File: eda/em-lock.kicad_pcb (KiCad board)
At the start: 2 copper layers, 75 x 75 mm, 62 parts, among them CON1 BARREL_JACK, P1 BTN_CALL, P10 EXT_LED_CONN, P2 BTN_OPEN, P3 BOOT_SEL_CONN, P4 LOCK_CONN, P5 PWR_SELECT, P6 PWR_SW_CONN, P7 SWD_CONN, P8 ESP8266_CONN, P9 USB_B, Q1 Q_NMOS_DGS, Q2 MMBT3906, Q3 MMBT3906, Q4 MMBT3906, SW1 RST_BTN, U1 74LVC2G14, U2 STM32F103C8Tx, U3 LD1117S33CTR, Y1 8MHz

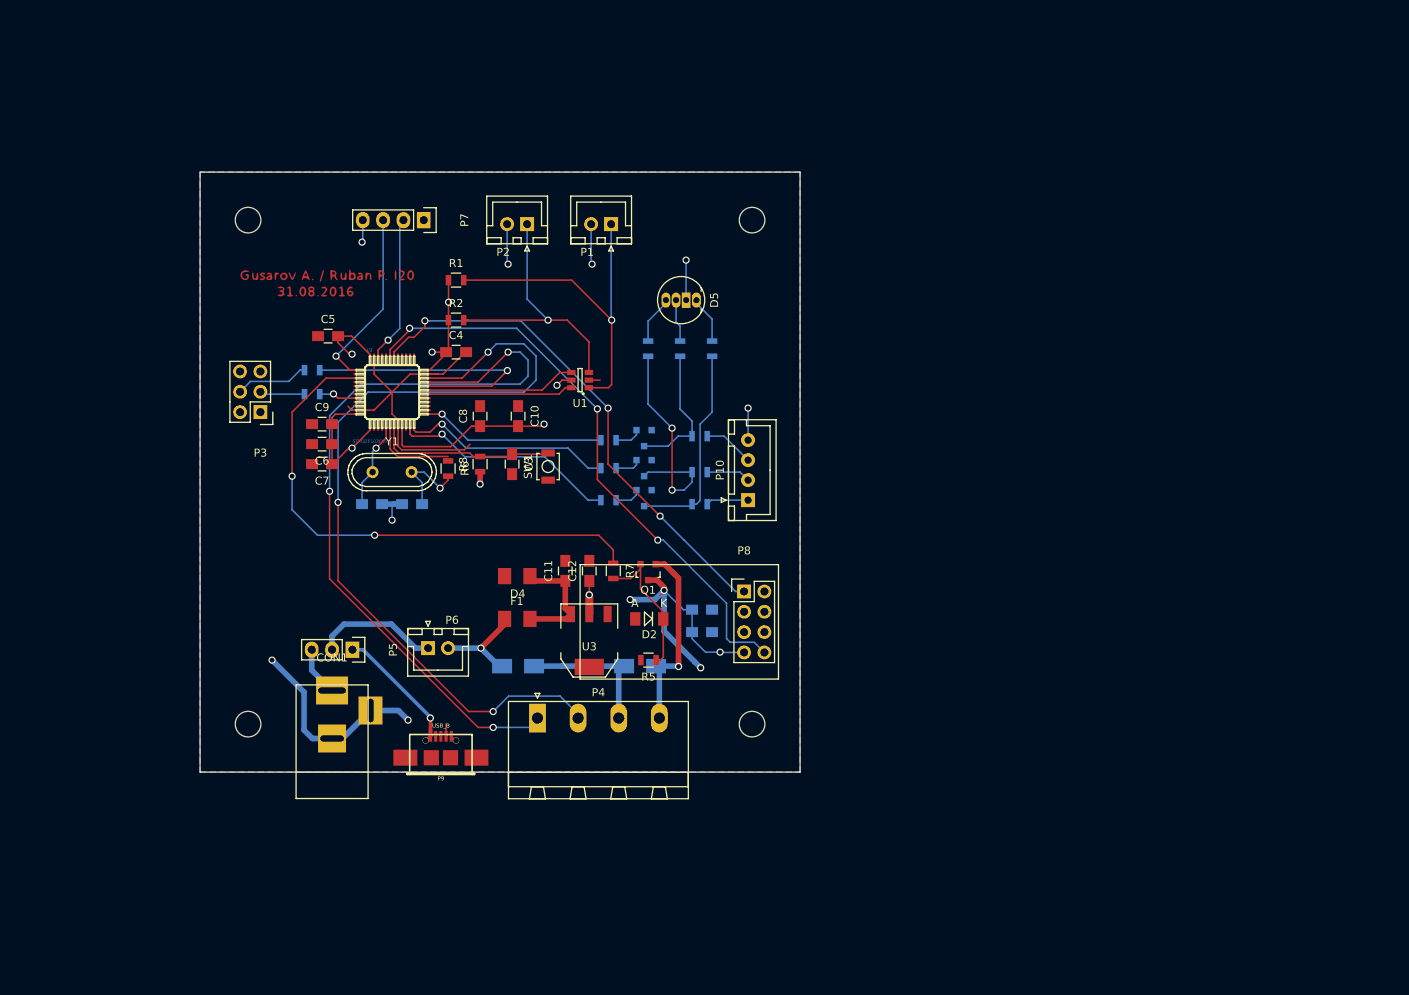
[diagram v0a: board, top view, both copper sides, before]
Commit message: refs #41563 fix stable schematics version
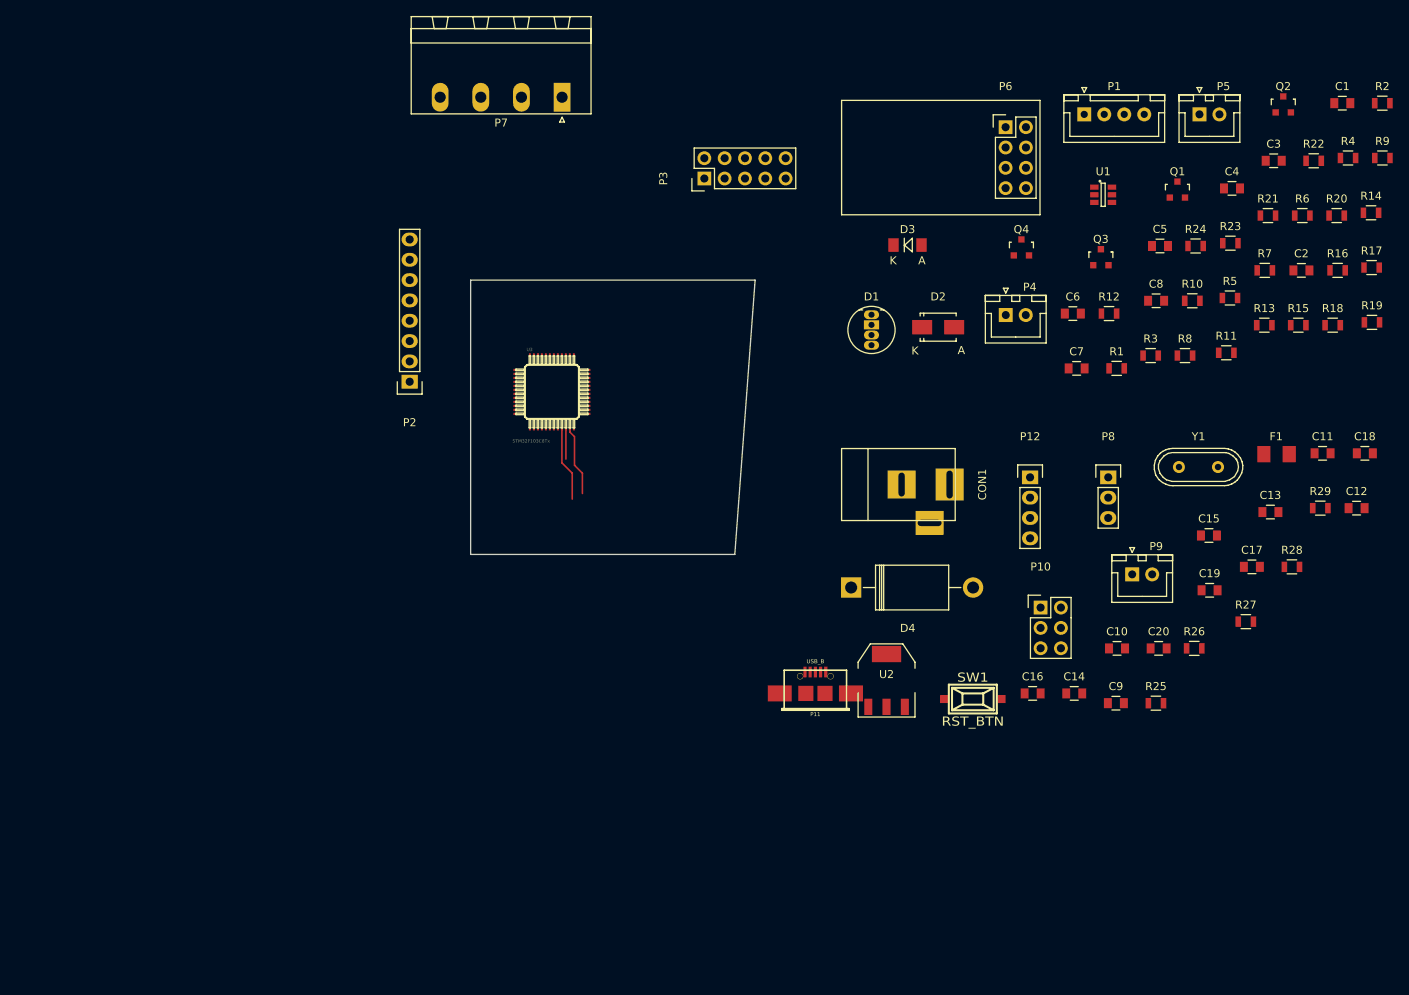
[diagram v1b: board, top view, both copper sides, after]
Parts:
- removed D5: LED_RCBG, I20:LED-RGB-5MM_Common_Cathode
- removed G1: LOGO, common_parts:logo_2016
- removed HOLE1, HOLE2, HOLE3, HOLE4: MountingHole_3.2mm_M3, Mounting_Holes:MountingHole_3.2mm_M3
- added C15: 2pF, I20:C_0805, F.Cu at (176.1, 95.4)
- added C16: 100nF, I20:C_0805, F.Cu at (154.1, 115.2)
- added C17: 100nF, I20:C_0805, F.Cu at (181.5, 99.3)
- added C18: 100nF, I20:C_0805, F.Cu at (195.6, 85.2)
- added C19: 10uF, I20:C_0805, F.Cu at (176.2, 102.3)
- added C20: 1uF, I20:C_0805, F.Cu at (169.8, 109.5)
- added P11: USB_B, I20:conn_usb_B_micro_smd-2, F.Cu at (126.9, 115.2)
- added P12: SWD_CONN, I20:Pin_Header_Straight_1x04, F.Cu at (153.8, 88.2)
- added R18: 4.7k, I20:R_0805, F.Cu at (191.6, 69.1)
- added R19: 4.7k, I20:R_0805, F.Cu at (196.5, 68.8)
- added R20: 4.7k, I20:R_0805, F.Cu at (192.1, 55.4)
- added R21: 4.7k, I20:R_0805, F.Cu at (183.5, 55.4)
- added R22: 0, I20:R_0805, F.Cu at (189.2, 48.6)
- added R23: 10k, I20:R_0805, F.Cu at (178.8, 58.9)
- added R24: 240, I20:R_0805, F.Cu at (174.4, 59.2)
- added R25: 10k, I20:R_0805, F.Cu at (169.5, 116.4)
- added R26: 10k, I20:R_0805, F.Cu at (174.3, 109.5)
- added R27: 10k, I20:R_0805, F.Cu at (180.7, 106.2)
- added R28: 0R, I20:R_0805, F.Cu at (186.5, 99.3)
- added R29: 0, I20:R_0805, F.Cu at (190.0, 92.0)
- C1: value 2pF -> 100nF; footprint I20:C_0805_HandSoldering -> I20:C_0805; moved to F.Cu
- C10: value 1uF -> 100nF; footprint I20:C_0805_HandSoldering -> I20:C_0805
- C11, C12, C3, C7: footprint I20:C_0805_HandSoldering -> I20:C_0805
- C13: value 10uF -> 100nF; footprint I20:C_0805_HandSoldering -> I20:C_0805; moved to F.Cu
- C14: value 100nF -> 2pF; footprint I20:C_0805_HandSoldering -> I20:C_0805; moved to F.Cu
- C2: value 2pF -> 10uF; footprint I20:C_0805_HandSoldering -> I20:C_0805; moved to F.Cu
- C4, C5: value 100nF -> 0; footprint I20:C_0805_HandSoldering -> I20:C_0805
- C6, C8: value 100nF -> 10uF; footprint I20:C_0805_HandSoldering -> I20:C_0805
- C9: value 10uF -> 100nF; footprint I20:C_0805_HandSoldering -> I20:C_0805
- D1: value M7 -> LED_RCBG; footprint I20:SMA_Standard -> I20:LED-RGB-5MM_Common_Cathode; moved to F.Cu
- D2: value ZENER-MOSFET-GATE -> M7; footprint I20:MiniMELF_Standard -> I20:SMA_Standard
- D3: value D_Schottky -> ZENER-MOSFET-GATE; footprint I20:SMA_Standard -> I20:MiniMELF_Standard; moved to F.Cu
- D4: footprint I20:Fuse_SMD1206_Wave -> Diodes_ThroughHole:Diode_DO-201AD_Horizontal_RM15
- P1: value BTN_CALL -> EXT_LED_CONN; footprint I20:JST_XH_B02B-XH-A_02x2.50mm_Straight -> I20:JST_XH_B04B-XH-A_04x2.50mm_Straight
- P10: value EXT_LED_CONN -> BOOT_SEL_CONN; footprint I20:JST_XH_B04B-XH-A_04x2.50mm_Straight -> I20:Pin_Header_Straight_2x03
- P2: value BTN_OPEN -> RC522A; footprint I20:JST_XH_B02B-XH-A_02x2.50mm_Straight -> Pin_Headers:Pin_Header_Straight_1x08
- P3: value BOOT_SEL_CONN -> RC522B; footprint I20:Pin_Header_Straight_2x03 -> Pin_Headers:Pin_Header_Straight_2x05
- P4: value LOCK_CONN -> BTN_OPEN; footprint I20:PhoenixContact_MSTBA-G_04x5.08mm_Angled -> I20:JST_XH_B02B-XH-A_02x2.50mm_Straight
- P5: value PWR_SELECT -> BTN_CALL; footprint I20:Pin_Header_Straight_1x03 -> I20:JST_XH_B02B-XH-A_02x2.50mm_Straight
- P6: value PWR_SW_CONN -> ESP8266_CONN; footprint I20:JST_XH_B02B-XH-A_02x2.50mm_Straight -> I20:ESP8266_CONN
- P7: value SWD_CONN -> LOCK_CONN; footprint I20:Pin_Header_Straight_1x04 -> I20:PhoenixContact_MSTBA-G_04x5.08mm_Angled
- P8: value ESP8266_CONN -> PWR_SELECT; footprint I20:ESP8266_CONN -> I20:Pin_Header_Straight_1x03
- P9: value USB_B -> PWR_SW_CONN; footprint I20:conn_usb_B_micro_smd-2 -> I20:JST_XH_B02B-XH-A_02x2.50mm_Straight
- Q1: value Q_NMOS_DGS -> MMBT3906
- Q2, Q3, R11: moved to F.Cu
- Q4: value MMBT3906 -> Q_NMOS_DGS; moved to F.Cu
- R1: value 10k -> 10R
- R10: value 2k -> 82R; moved to F.Cu
- R12: value 82R -> 2k; moved to F.Cu
- R13: value 15R -> 2k; moved to F.Cu
- R14: value 10R -> 10k; moved to F.Cu
- R15: value 82R -> 10k; moved to F.Cu
- R16: value 15R -> 0; moved to F.Cu
- R17: value 10R -> 0; moved to F.Cu
- R2: value 10k -> 15R
- R3: value 10k -> 82R; moved to F.Cu
- R4: value 10k -> 4.7k; moved to F.Cu
- R5, R8: value 10k -> 4.7k
- R6: value 0R -> 10R
- R7: value 240 -> 4.7k
- R9: value 2k -> 15R; moved to F.Cu
- SW1: footprint Buttons_Switches_SMD:SW_SPST_B3U-1000P -> I20:smd_push
- U2: value STM32F103C8Tx -> LD1117S33CTR; footprint I20:SparkFun-LQFP-48 -> I20:SOT-223
- U3: value LD1117S33CTR -> STM32F103C8Tx; footprint I20:SOT-223 -> I20:SparkFun-LQFP-48
- moved R4 132.2 mm to (193.5, 48.2)
- moved C1 131.2 mm to (192.8, 41.4)
- moved P5 125.3 mm to (174.9, 42.8), turned to 0 degrees
- moved R2 118.9 mm to (197.8, 41.4)
- moved C2 114.9 mm to (187.7, 62.3), turned to 0 degrees
- moved R6 111.4 mm to (187.8, 55.4), turned to 0 degrees
- moved R9 105.8 mm to (197.8, 48.2), turned to 0 degrees
- moved C9 105.2 mm to (164.5, 116.4)
- moved R3 104.9 mm to (168.8, 72.9)
- moved C5 104.6 mm to (170.0, 59.2)
- moved C3 102.5 mm to (184.2, 48.6), turned to 0 degrees
- moved Y1 100.8 mm to (174.8, 86.9)
- moved C4 99.1 mm to (179.0, 52.0)
- moved P6 98.0 mm to (155.0, 48.2)
- moved F1 97.1 mm to (184.6, 85.3)
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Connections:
- C1 pad 1: /OSC_IN -> VCC
- C1 pad 2: GND -> GNDD
- C10 pad 1: GND -> VCC
- C10 pad 2: VCC -> GND
- C11 pad 1: /LDO_IN -> /stm32f103c8/LDO_IN
- C14 pad 1: GND -> /stm32f103c8/PD0/RCC_OSC_IN
- C14 pad 2: VCC -> Net-(C14-Pad2)
- C2 pad 1: /OSC_OUT -> VCC
- C2 pad 2: GND -> GNDD
- C3 pad 1: /NRST -> VCC
- C3 pad 2: GND -> GNDD
- C4 pad 1: VCC -> GNDD
- C4 pad 2: GND -> Net-(C4-Pad2)
- C5 pad 1: GND -> GNDD
- C5 pad 2: VCC -> Net-(C5-Pad2)
- C6 pad 2: GND -> GNDD
- C7 pad 1: VCC -> GNDD
- C7 pad 2: GND -> VCC
- C8 pad 1: VCC -> GNDD
- C8 pad 2: GND -> VCC
- C9 pad 1: GND -> /stm32f103c8/NRST
- C9 pad 2: VCC -> GND
- CON1 pad 1: /12V_EXT -> /stm32f103c8/12V_EXT
- D1 pad 1: EM_LOCK -> Net-(D1-Pad1)
- D1 pad 2: /LOCK_GND -> GND
- D2 pad 1: Net-(D2-Pad1) -> EM_LOCK
- D2 pad 2: GND -> LOCK_GND
- D3 pad 1: EM_LOCK -> Net-(D3-Pad1)
- D3 pad 2: /PWR_UNFUSED -> GND
- D4 pad 1: /LDO_IN -> /stm32f103c8/LDO_IN
- F1 pad 1: /PWR_UNFUSED -> Net-(F1-Pad1)
- F1 pad 2: /LDO_IN -> Net-(F1-Pad2)
- P1 pad 2: GND -> Net-(P1-Pad2)
- P10 pad 2: Net-(P10-Pad2) -> Net-(P10-Pad1)
- P10 pad 4: GND -> Net-(P10-Pad4)
- P2 pad 1: Net-(P2-Pad1) -> /PB5_RC522A_CS
- P2 pad 2: GND -> /PB13_SPI2_SCK
- P3 pad 1: VCC -> /PB6_RC522B_CS
- P3 pad 2: VCC -> /PB13_SPI2_SCK
- P3 pad 3: Net-(P3-Pad3) -> /PB15_SPI2_MOSI
- P3 pad 4: Net-(P3-Pad4) -> /PB14_SPI2_MISO
- P3 pad 5: GND -> /PB9_RC522B_IRQ
- P3 pad 6: GND -> GNDD
- P4 pad 1: /UART_EXT_TX -> Net-(P4-Pad1)
- P4 pad 2: /UART_EXT_RX -> GNDD
- P5 pad 1: +5V -> Net-(P5-Pad1)
- P5 pad 2: Net-(P5-Pad2) -> GNDD
- P6 pad 1: Net-(P5-Pad2) -> (no net)
- P6 pad 2: /PWR_UNFUSED -> VCC
- P7 pad 1: VCC -> (no net)
- P7 pad 2: Net-(P7-Pad2) -> (no net)
- P7 pad 3: Net-(P7-Pad3) -> EM_LOCK
- P7 pad 4: GND -> LOCK_GND
- P8 pad 1: /UART_INT_TX -> /stm32f103c8/12V_EXT
- P8 pad 2: VCC -> Net-(F1-Pad2)
- P8 pad 3: Net-(P8-Pad3) -> +5V
- P9 pad 1: +5V -> /stm32f103c8/LDO_IN
- Q1 pad 1: /LOCK_GND -> Net-(Q1-Pad1)
- Q1 pad 2: Net-(D2-Pad1) -> VCC
- Q1 pad 3: GND -> Net-(Q1-Pad3)
- Q4 pad 1: Net-(Q4-Pad1) -> LOCK_GND
- Q4 pad 2: VCC -> Net-(D3-Pad1)
- Q4 pad 3: Net-(Q4-Pad3) -> GND
- R1 pad 1: VCC -> Net-(Q1-Pad3)
- R1 pad 2: Net-(P1-Pad1) -> Net-(P1-Pad3)
- R10 pad 1: Net-(Q3-Pad1) -> Net-(Q3-Pad3)
- R10 pad 2: /PIN_GREEN -> Net-(D1-Pad1)
- R11 pad 1: Net-(Q4-Pad1) -> Net-(Q1-Pad1)
- R11 pad 2: /PIN_BLUE -> (no net)
- R12 pad 1: Net-(Q2-Pad3) -> Net-(Q2-Pad1)
- R12 pad 2: Net-(D5-Pad1) -> (no net)
- R13 pad 1: Net-(Q3-Pad3) -> Net-(Q3-Pad1)
- R13 pad 2: Net-(D5-Pad4) -> (no net)
- R14 pad 1: Net-(Q4-Pad3) -> VCC
- R14 pad 2: Net-(D5-Pad3) -> Net-(P4-Pad1)
- R15 pad 1: Net-(Q2-Pad3) -> VCC
- R15 pad 2: Net-(P10-Pad1) -> Net-(P5-Pad1)
- R16 pad 1: Net-(Q3-Pad3) -> Net-(C4-Pad2)
- R16 pad 2: Net-(P10-Pad2) -> Net-(P4-Pad1)
- R17 pad 1: Net-(Q4-Pad3) -> Net-(C5-Pad2)
- R17 pad 2: Net-(P10-Pad3) -> Net-(P5-Pad1)
- R2 pad 1: VCC -> Net-(Q2-Pad3)
- R2 pad 2: Net-(P2-Pad1) -> Net-(P1-Pad2)
- R3 pad 1: Net-(P3-Pad3) -> Net-(Q3-Pad3)
- R3 pad 2: /BOOT0 -> Net-(P1-Pad1)
- R4 pad 1: Net-(P3-Pad4) -> VCC
- R4 pad 2: /BOOT1 -> /PB5_RC522A_CS
- R5 pad 1: Net-(D2-Pad1) -> VCC
- R5 pad 2: GND -> /PB14_SPI2_MISO
- R6 pad 1: Net-(R6-Pad1) -> Net-(Q1-Pad3)
- R6 pad 2: /OSC_OUT -> Net-(D1-Pad3)
- R7 pad 1: /LOCK_OPEN -> GNDD
- R7 pad 2: Net-(D2-Pad1) -> /PB8_RC522A_IRQ
- R8 pad 2: /NRST -> /PB7_RC522_RST
- R9 pad 1: Net-(Q2-Pad1) -> Net-(Q2-Pad3)
- R9 pad 2: /PIN_RED -> Net-(D1-Pad4)
- SW1 pad 2: /NRST -> /stm32f103c8/NRST
- U1 pad 1: Net-(P1-Pad1) -> Net-(C4-Pad2)
- U1 pad 3: Net-(P2-Pad1) -> Net-(C5-Pad2)
- U1 pad 4: /BTN_CALL -> (no net)
- U1 pad 6: /BTN_OPEN -> (no net)
- U2 pad 1: VCC -> GND
- U2 pad 2: Net-(U2-Pad2) -> VCC
- U2 pad 3: Net-(U2-Pad3) -> /stm32f103c8/LDO_IN
- U2 pad 4: Net-(U2-Pad4) -> (no net)
- U3 pad 1: GND -> VCC
- U3 pad 2: VCC -> (no net)
- U3 pad 3: /LDO_IN -> (no net)
- Y1 pad 1: /OSC_IN -> /stm32f103c8/PD0/RCC_OSC_IN
- Y1 pad 2: /OSC_OUT -> Net-(C15-Pad1)
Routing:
- net GND: track 131.9 -> 0.00 mm, vias 12 -> 0
- net /UART_EXT_RX: track 105.2 -> 0.00 mm, vias 3 -> 0
- net /UART_EXT_TX: track 98.5 -> 0.00 mm, vias 3 -> 0
- net /UART_INT_RX: track 73.6 -> 0.00 mm, vias 3 -> 0
- net /LOCK_OPEN: track 66.1 -> 0.00 mm, vias 2 -> 0
- net /UART_INT_TX: track 64.7 -> 0.00 mm, vias 3 -> 0
- net (no net): track 0.00 -> 59.6 mm
- net VCC: track 68.4 -> 9.69 mm, vias 8 -> 0
- net Net-(P1-Pad1): track 43.8 -> 0.00 mm, vias 1 -> 0
- net /BOOT1: track 34.5 -> 0.00 mm, vias 1 -> 0
- net Net-(P2-Pad1): track 34.3 -> 0.00 mm, vias 1 -> 0
- net /PIN_RED: track 28.5 -> 0.00 mm, vias 1 -> 0
- net Net-(Q3-Pad3): track 28.3 -> 0.00 mm, vias 2 -> 0
- net /PIN_GREEN: track 26.6 -> 0.00 mm, vias 1 -> 0
- net Net-(Q2-Pad3): track 25.9 -> 0.00 mm
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- removed copper zone on F.Cu, net GND
- removed copper zone on B.Cu, net VCC
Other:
- board size 75 x 75 mm -> 35.6 x 34.3 mm

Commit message: refs #41563 pcb projecting half-done
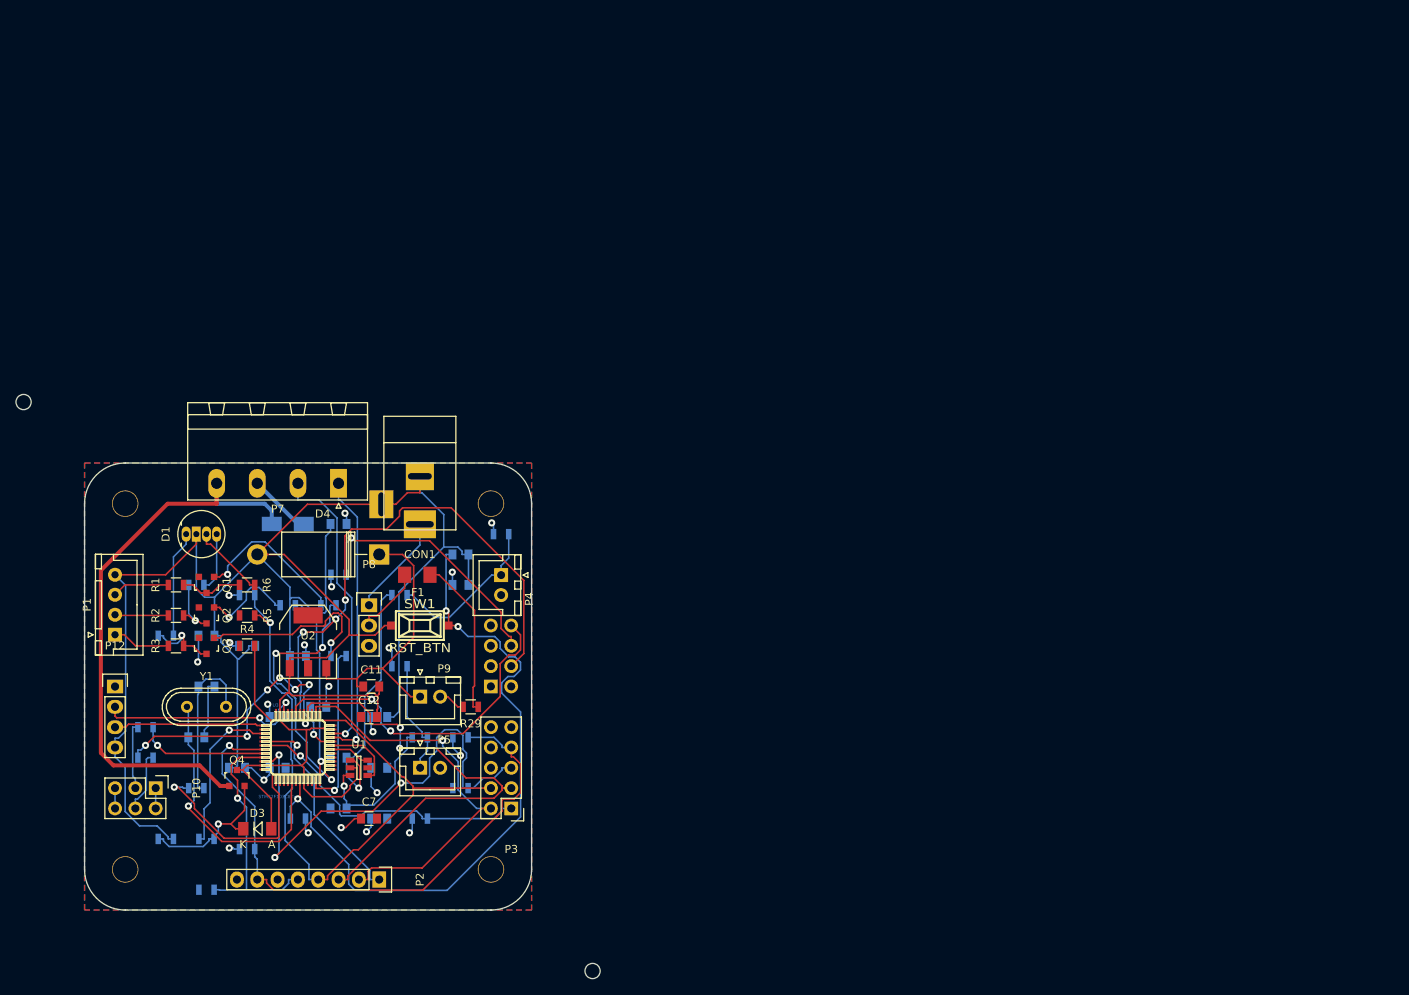
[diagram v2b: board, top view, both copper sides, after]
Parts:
- removed P11: USB_B, I20:conn_usb_B_micro_smd-2
- added H1: MountingHole_3.1mm, I20:MountingHole_3.1mm, F.Cu at (40.6, 91.4)
- added H2: MountingHole_3.1mm, I20:MountingHole_3.1mm, F.Cu at (86.4, 91.4)
- added H3: MountingHole_3.1mm, I20:MountingHole_3.1mm, F.Cu at (86.4, 137.2)
- added H4: MountingHole_3.1mm, I20:MountingHole_3.1mm, F.Cu at (40.6, 137.2)
- added H5: MountingHole_1.9mm, I20:MountingHole_1.9mm, F.Cu at (99.1, 149.9)
- added H6: MountingHole_1.9mm, I20:MountingHole_1.9mm, F.Cu at (27.9, 78.7)
- C1, C10, C13, C14, C15, C16, C17, C18, C19, C2, C20, C3, C4, C5, C6, C8, C9, D2, R10, R11, R12, R13, R14, R15, R16, R17, R18, R19, R20, R21, R22, R23, R24, R25, R26, R27, R28, R7, R8, R9: moved to B.Cu
- F1: value F_Small -> 3A
- P6: footprint I20:ESP8266_CONN -> ESP8266_CONN; moved to B.Cu
- moved R2 163.8 mm to (47.0, 105.4), turned to 180 degrees
- moved R9 157.6 mm to (49.5, 101.6)
- moved C1 153.6 mm to (59.7, 118.1)
- moved R7 153.3 mm to (50.8, 139.7)
- moved R23 152.5 mm to (45.7, 133.3)
- moved R4 150.5 mm to (55.9, 109.2)
- moved Q2 149.0 mm to (50.8, 105.4), turned to 180 degrees
- moved R19 144.7 mm to (55.9, 102.9)
- moved R24 144.2 mm to (50.8, 133.3)
- moved C2 142.3 mm to (59.7, 124.5)
- moved R6 139.7 mm to (55.9, 101.6)
- moved R28 139.7 mm to (49.5, 127.0)
- moved R27 138.6 mm to (43.2, 123.2)
- moved P1 137.5 mm to (39.4, 107.8), turned to 90 degrees
- moved C3 135.1 mm to (72.4, 124.5)
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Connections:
- P2 pad 1: /PB5_RC522A_CS -> PB5_RC522A_CS
- P2 pad 2: /PB13_SPI2_SCK -> PB13_SPI2_SCK
- P2 pad 3: /PB15_SPI2_MOSI -> PB15_SPI2_MOSI
- P2 pad 4: /PB14_SPI2_MISO -> PB14_SPI2_MISO
- P2 pad 5: /PB8_RC522A_IRQ -> PB8_RC522A_IRQ
- P2 pad 7: /PB7_RC522_RST -> PB7_RC522_RST
- P3 pad 1: /PB6_RC522B_CS -> PB6_RC522B_CS
- P3 pad 10: (no net) -> Net-(P3-Pad10)
- P3 pad 2: /PB13_SPI2_SCK -> PB13_SPI2_SCK
- P3 pad 3: /PB15_SPI2_MOSI -> PB15_SPI2_MOSI
- P3 pad 4: /PB14_SPI2_MISO -> PB14_SPI2_MISO
- P3 pad 5: /PB9_RC522B_IRQ -> PB9_RC522B_IRQ
- P3 pad 7: /PB7_RC522_RST -> PB7_RC522_RST
- P3 pad 9: (no net) -> Net-(P3-Pad9)
- P6 pad 1: (no net) -> UART_INT_TX
- P6 pad 3: (no net) -> Net-(P6-Pad3)
- P6 pad 4: (no net) -> ESP_RESET
- P6 pad 5: (no net) -> Net-(P6-Pad5)
- P6 pad 8: (no net) -> UART_INT_RX
- P7 pad 1: (no net) -> UART_EXT_TX
- P7 pad 2: (no net) -> UART_EXT_RX
- P8 pad 3: +5V -> Net-(P8-Pad3)
- R11 pad 2: (no net) -> PIN_BLUE
- R12 pad 2: (no net) -> PIN_GREEN
- R13 pad 2: (no net) -> PIN_RED
- R18 pad 2: /PB6_RC522B_CS -> PB6_RC522B_CS
- R19 pad 2: /PB14_SPI2_MISO -> PB14_SPI2_MISO
- R20 pad 2: /PB9_RC522B_IRQ -> PB9_RC522B_IRQ
- R21 pad 2: /PB7_RC522_RST -> PB7_RC522_RST
- R24 pad 1: (no net) -> LOCK_OPEN
- R4 pad 2: /PB5_RC522A_CS -> PB5_RC522A_CS
- R5 pad 2: /PB14_SPI2_MISO -> PB14_SPI2_MISO
- R7 pad 2: /PB8_RC522A_IRQ -> PB8_RC522A_IRQ
- R8 pad 2: /PB7_RC522_RST -> PB7_RC522_RST
- U1 pad 4: (no net) -> BTN_CALL
- U1 pad 6: (no net) -> BTN_OPEN
- U3 pad 10: (no net) -> Net-(U3-Pad10)
- U3 pad 11: (no net) -> PIN_RED
- U3 pad 12: (no net) -> PIN_GREEN
- U3 pad 13: (no net) -> PIN_BLUE
- U3 pad 14: (no net) -> Net-(U3-Pad14)
- U3 pad 15: (no net) -> Net-(U3-Pad15)
- U3 pad 16: (no net) -> Net-(U3-Pad16)
- U3 pad 17: (no net) -> Net-(U3-Pad17)
- U3 pad 18: (no net) -> BTN_OPEN
- U3 pad 19: (no net) -> BTN_CALL
- U3 pad 2: (no net) -> Net-(U3-Pad2)
- U3 pad 21: (no net) -> UART_EXT_TX
- U3 pad 22: (no net) -> UART_EXT_RX
- U3 pad 25: (no net) -> Net-(U3-Pad25)
- U3 pad 26: (no net) -> PB13_SPI2_SCK
- U3 pad 27: (no net) -> PB14_SPI2_MISO
- U3 pad 28: (no net) -> PB15_SPI2_MOSI
- U3 pad 29: (no net) -> ESP_RESET
- U3 pad 3: (no net) -> Net-(U3-Pad3)
- U3 pad 30: (no net) -> UART_INT_TX
- U3 pad 31: (no net) -> UART_INT_RX
- U3 pad 32: (no net) -> Net-(U3-Pad32)
- U3 pad 33: (no net) -> Net-(U3-Pad33)
- U3 pad 38: (no net) -> Net-(U3-Pad38)
- U3 pad 39: (no net) -> LOCK_OPEN
- U3 pad 4: (no net) -> Net-(U3-Pad4)
- U3 pad 40: (no net) -> Net-(U3-Pad40)
- U3 pad 41: (no net) -> PB5_RC522A_CS
- U3 pad 42: (no net) -> PB6_RC522B_CS
- U3 pad 43: (no net) -> PB7_RC522_RST
- U3 pad 45: (no net) -> PB8_RC522A_IRQ
- U3 pad 46: (no net) -> PB9_RC522B_IRQ
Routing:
- net GND: track 0.00 -> 292.6 mm
- net PB14_SPI2_MISO: track 0.00 -> 87.3 mm, vias 0 -> 1
- net /stm32f103c8/NRST: track 0.00 -> 87.0 mm, vias 0 -> 3
- net PB7_RC522_RST: track 0.00 -> 75.4 mm, vias 0 -> 1
- net LOCK_GND: track 0.00 -> 72.5 mm
- net ESP_RESET: track 0.00 -> 68.5 mm, vias 0 -> 4
- net PB9_RC522B_IRQ: track 0.00 -> 62.2 mm, vias 0 -> 3
- net PB15_SPI2_MOSI: track 0.00 -> 60.0 mm, vias 0 -> 2
- net (no net): track 59.6 -> 0.00 mm
- net PB13_SPI2_SCK: track 0.00 -> 51.3 mm, vias 0 -> 1
- net UART_INT_RX: track 0.00 -> 42.5 mm, vias 0 -> 2
- net PB5_RC522A_CS: track 0.00 -> 39.1 mm, vias 0 -> 1
- net /stm32f103c8/PB2/BOOT1: track 0.00 -> 38.5 mm, vias 0 -> 7
- net UART_EXT_RX: track 0.00 -> 37.7 mm, vias 0 -> 1
- net PB6_RC522B_CS: track 0.00 -> 37.5 mm, vias 0 -> 1
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- added copper zone on B.Cu, net GNDD
- added copper zone on F.Cu, net VCC
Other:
- board size 35.6 x 34.3 mm -> 55.9 x 55.9 mm
- net class 3V3: via_drill 0.6 -> 0.4
- net class Default: via_drill 0.6 -> 0.4
- net class Power: trace_width 0.7 -> 0.5; via_drill 0.6 -> 0.4
- net class USB: via_drill 0.6 -> 0.4
- rule via_min_drill: 0.6 -> 0.4
